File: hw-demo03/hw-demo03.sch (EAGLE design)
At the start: 42 parts, among them IC3 MCP2562T, IC4 STM32F042, Q1 BTS500101TADATMA2, Q2 BTS500101TADATMA2, SW1+ VP0265840000G, SW2+ VP0265840000G

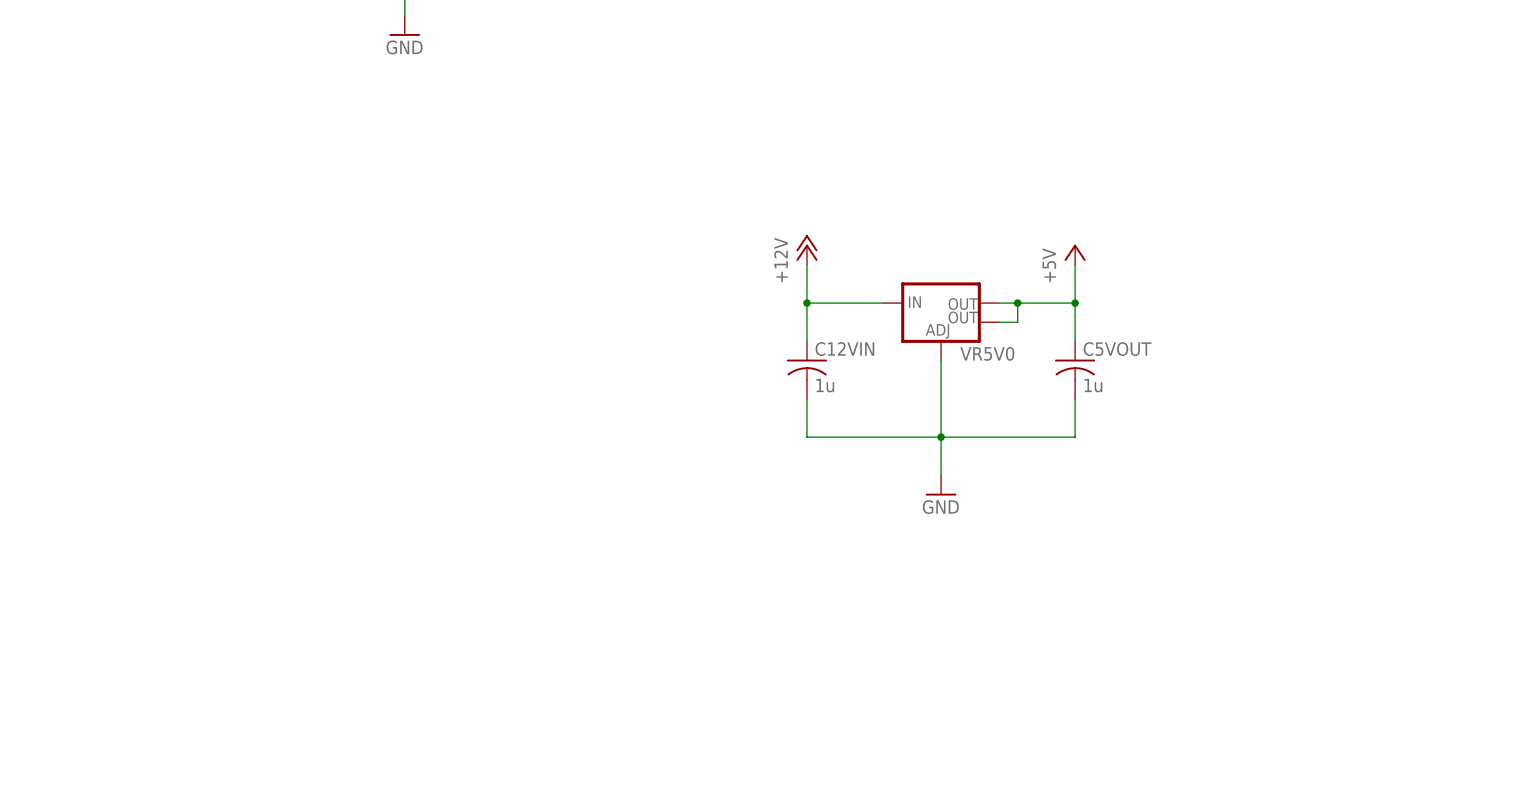
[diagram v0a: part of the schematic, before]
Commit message: footprint too big, will try something else
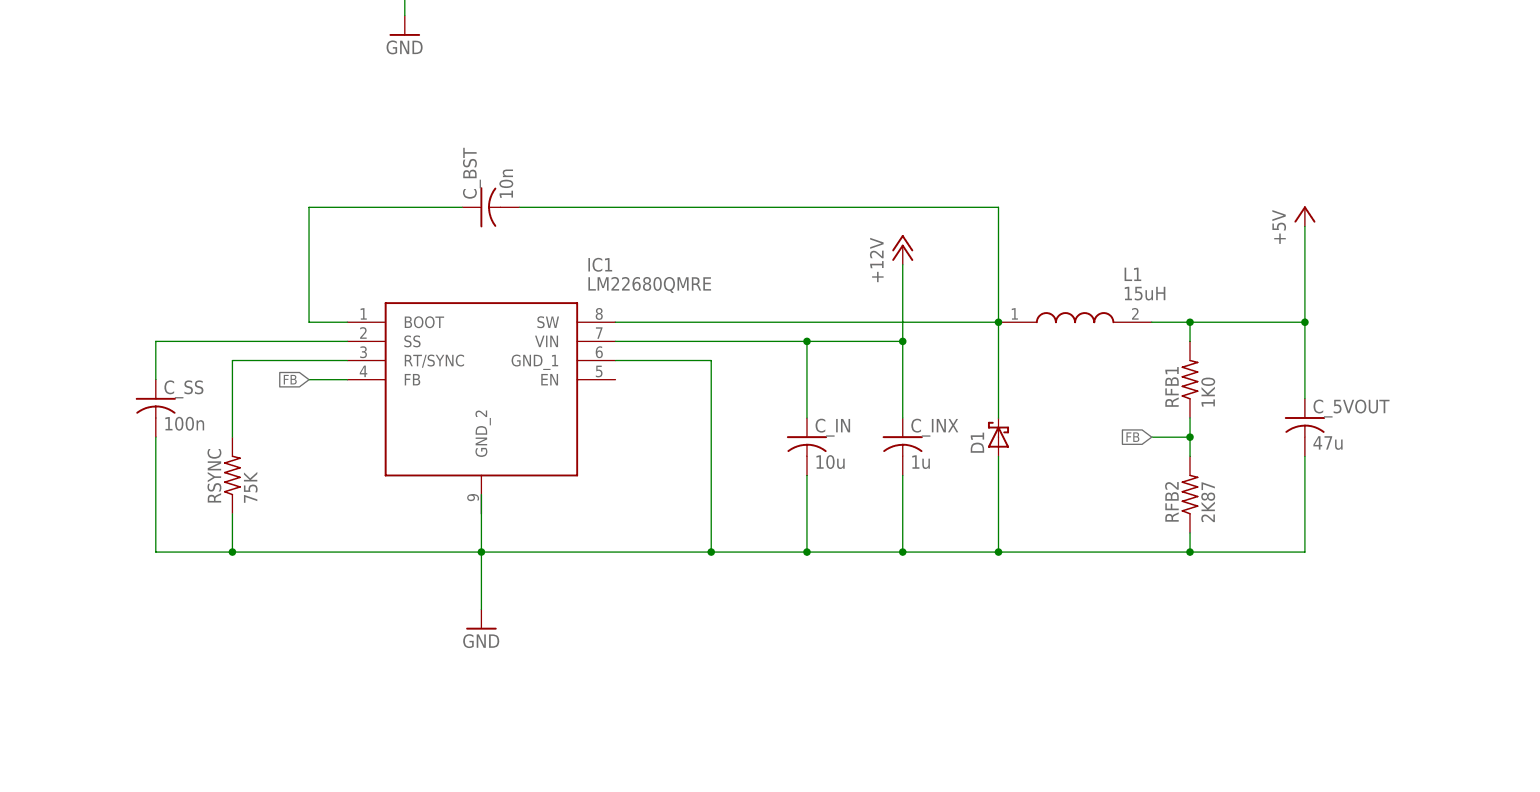
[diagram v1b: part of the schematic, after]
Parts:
- removed C12VIN: 1u, rcl:C-USC1206K
- removed C5VOUT: 1u, rcl:C-USC0805K
- removed VR5V0: (no value), SparkFun-PowerIC:V_REG_LM1117SOT223
- added C_5VOUT: 47u, rcl:C-USC1210K
- added C_BST: 10n, rcl:C-USC0805K
- added C_IN: 10u, rcl:C-USC1210K
- added C_INX: 1u, rcl:C-USC0805K
- added C_SS: 100n, rcl:C-USC0805K
- added D1: (no value), diode-special-packages:SCHOTTKY-SMB
- added IC1: LM22680QMRE, LM22680QMRE-ADJ_NOPB:LM22680QMRE-ADJ_NOPB
- added L1: 15uH, CLF7045NIT-150M-D:CLF7045NIT-150M-D
- added RFB1: 1K0, rcl:R-US_R0805
- added RFB2: 2K87, rcl:R-US_R0805
- added RSYNC: 75K, rcl:R-US_R0805
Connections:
- new net BOOST: C_BST.1, IC1.BOOT
- new net FB: IC1.FB, RFB1.1, RFB2.2
- new net SS: C_SS.1, IC1.SS
- new net SW: C_BST.2, D1.K, IC1.SW, L1.1
- new net SYNC: IC1.RT/SYNC, RSYNC.2
- net +12V: now also C_IN.1, C_INX.1, IC1.VIN; no longer C12VIN.1, VR5V0.IN
- net +5V: now also C_5VOUT.1, L1.2, RFB1.2; no longer C5VOUT.1, VR5V0.OUT, VR5V0.OUT@1
- net GND: now also C_5VOUT.2, C_IN.2, C_INX.2, C_SS.2, D1.A, IC1.GND_1, RFB2.1, RSYNC.1; no longer C12VIN.2, C5VOUT.2, VR5V0.ADJ
